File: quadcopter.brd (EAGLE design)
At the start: 196 x 196 mm, 65 parts, among them J1 ISP, U1 ATMEGA128RFA1

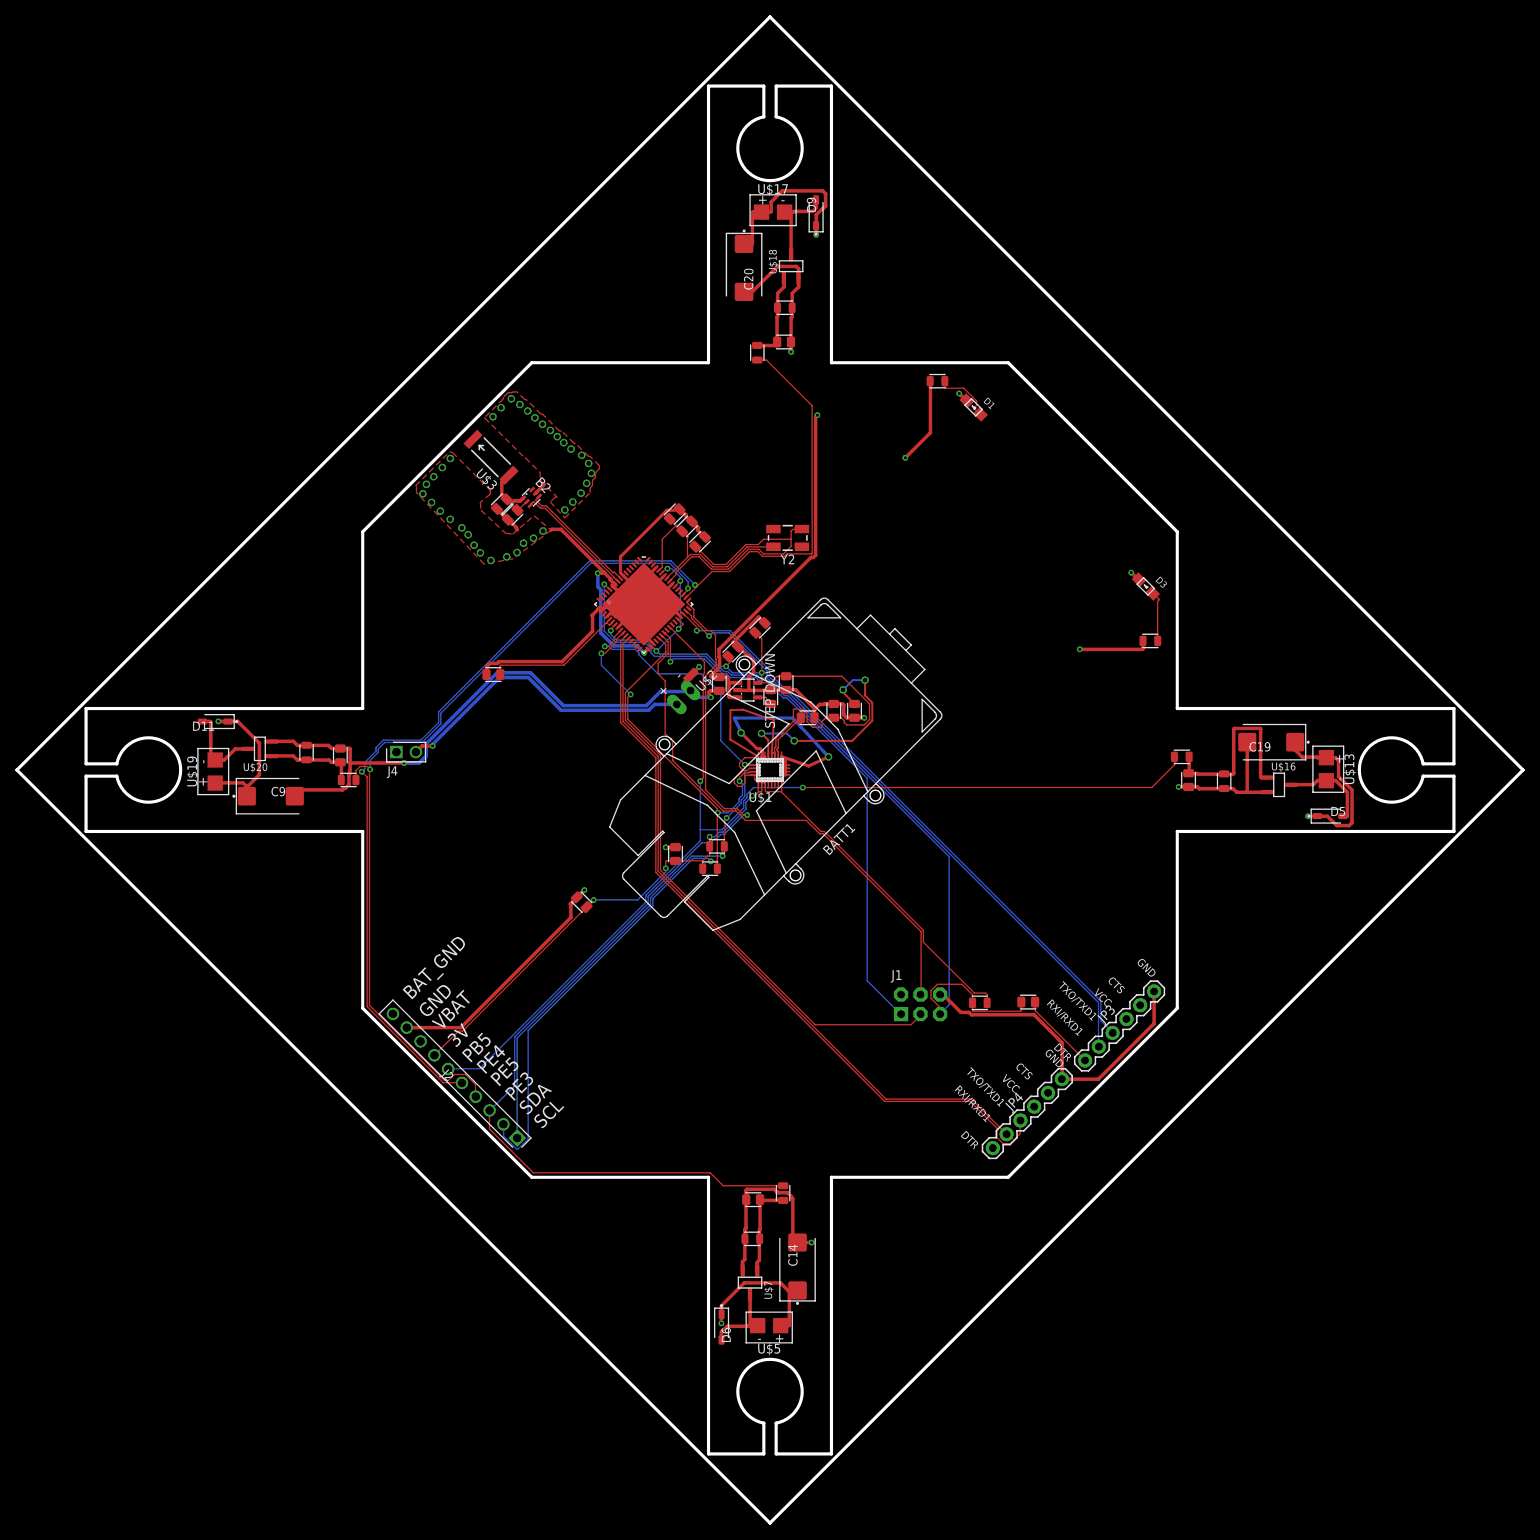
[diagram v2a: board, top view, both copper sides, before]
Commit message: worked on routing more, there are still lots of drc issues though
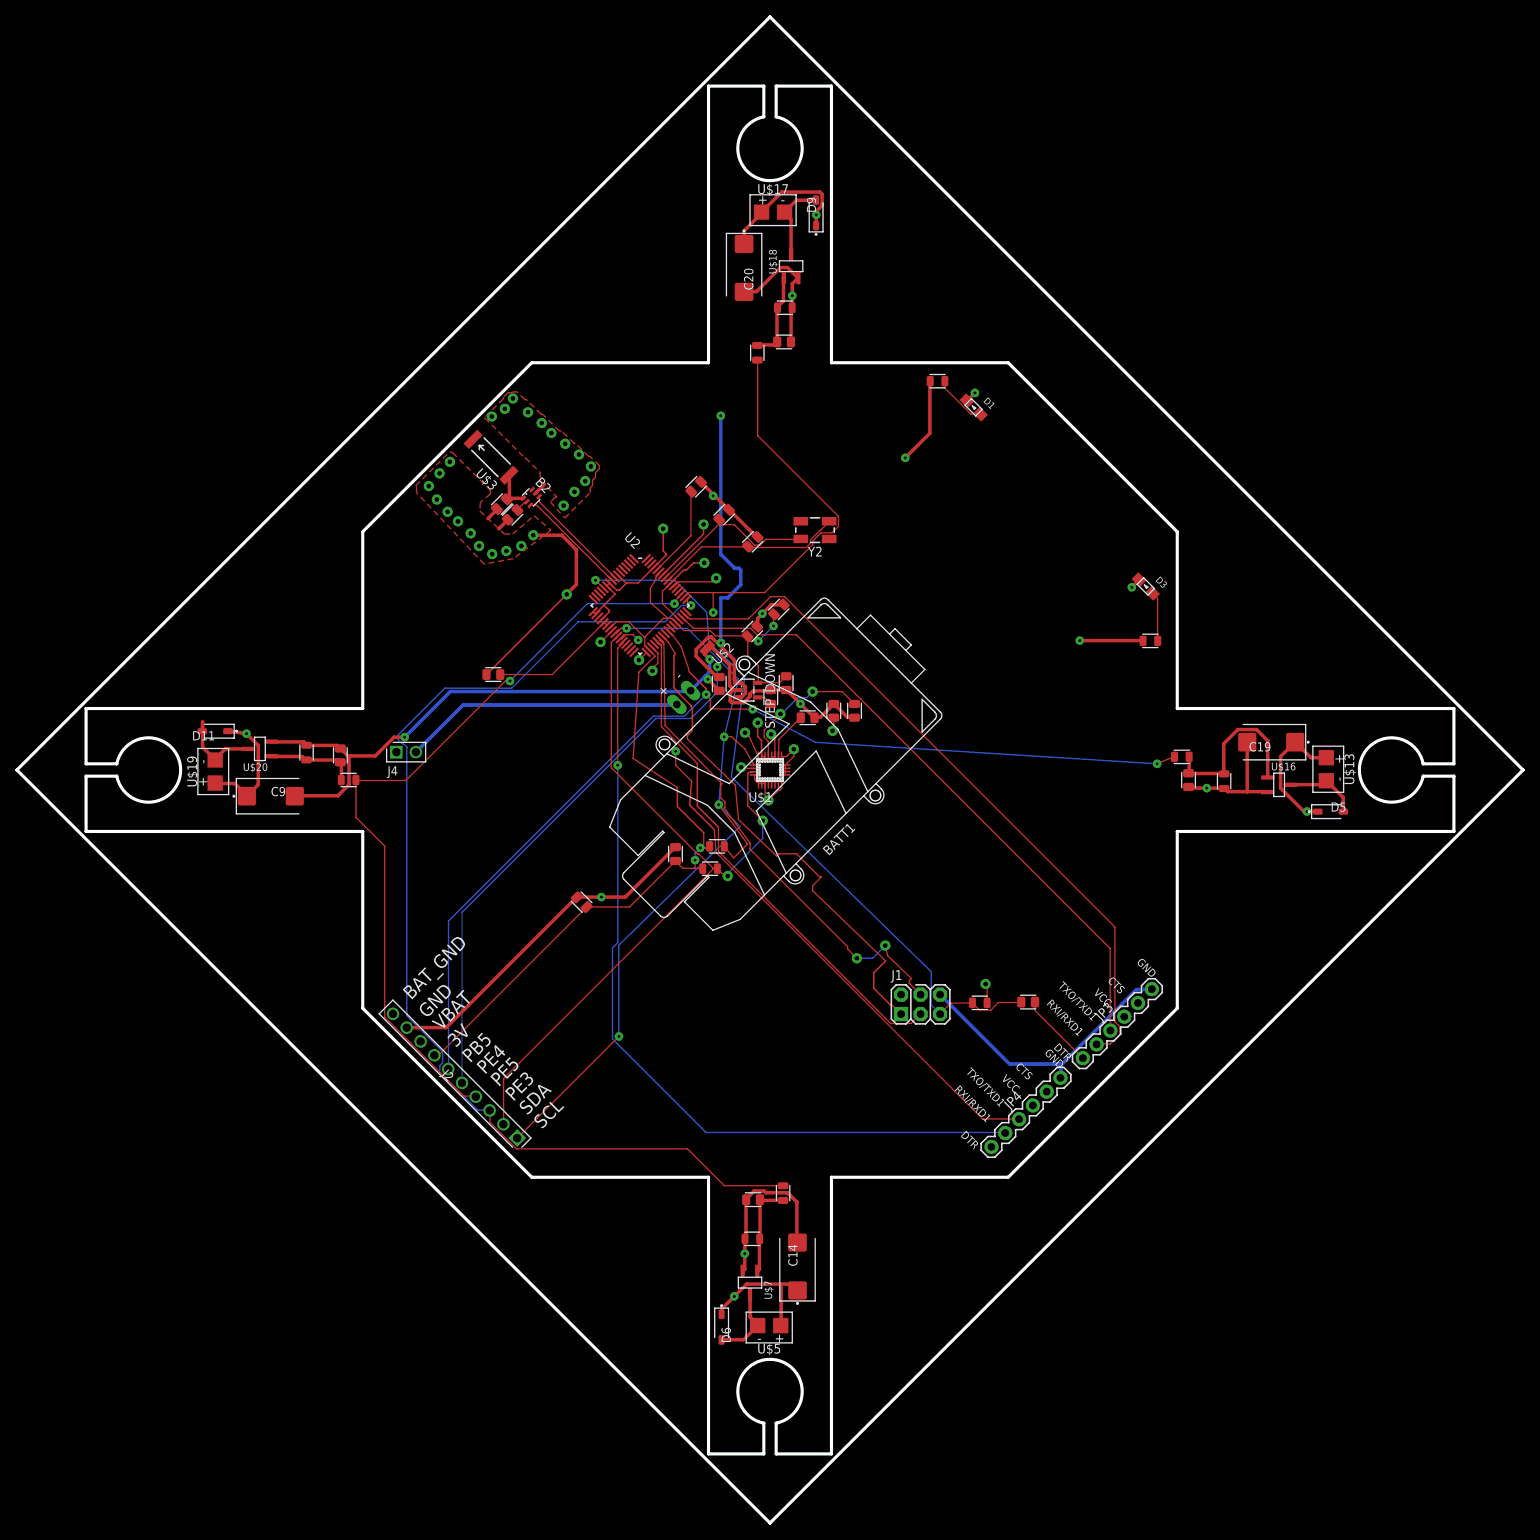
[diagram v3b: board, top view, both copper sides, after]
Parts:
- removed U1: ATMEGA128RFA1, SparkFun-DigitalIC:QFN-64
- added U2: ATMEGA128RFA1, quadparts_prebuilt:QFN-64
- J1: device SparkFun-Connectors:2X3-NS -> quadparts_prebuilt:2X3-NS
- moved C1 6.86 mm to (-2.24, 29.7)
- moved C2 5.06 mm to (-5.97, 33.2)
- moved C6 4.52 mm to (-9.61, 36.9)
- moved U$2 4.15 mm to (-8.15, 15.8)
- moved Y2 3.70 mm to (5.86, 31.2)
- moved C4 3.64 mm to (-2.30, 18.1)
- moved C3 3.43 mm to (1.15, 20.9)
- moved D11 1.25 mm to (-72.2, 5.05)
- moved D5 0.58 mm to (73.0, -5.42)
- moved JP3 0.42 mm to (40.7, -37.5)
- moved JP4 0.24 mm to (28.8, -49.0)
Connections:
- net 3V: now also U2.23, U2.34, U2.44, U2.54, U2.59; no longer U1.23, U1.34, U1.44, U1.54, U1.59
- net A0: now also U2.63; no longer U1.63
- net A1: now also U2.64; no longer U1.64
- net A2: now also U2.1; no longer U1.1
- net A3: now also U2.2; no longer U1.2
- net A4: now also U2.3; no longer U1.3
- net A5: now also U2.4; no longer U1.4
- net A6: now also U2.5; no longer U1.5
- net A7: now also U2.6; no longer U1.6
- net AREF: now also U2.62; no longer U1.62
- net AVDD: now also U2.60; no longer U1.60
- net DVDD: now also U2.21, U2.22; no longer U1.21, U1.22
- net GND: now also U2.10, U2.11, U2.17, U2.18, U2.20, U2.24, U2.33, U2.35, U2.45, U2.55, U2.58, U2.61, U2.7; no longer U1.10, U1.11, U1.17, U1.18, U1.20, U1.24, U1.33, U1.35, U1.45, U1.55, U1.58, U1.61, U1.65, U1.7
- net MISO: now also U2.39; no longer U1.39
- net MOSI: now also U2.38; no longer U1.38
- net N$3: now also U2.57; no longer U1.57
- net N$4: now also U2.56; no longer U1.56
- net PB4: now also U2.40; no longer U1.40
- net PB5: now also U2.41; no longer U1.41
- net PB6: now also U2.42; no longer U1.42
- net PB7: now also U2.43; no longer U1.43
- net PD4: now also U2.29; no longer U1.29
- net PD5: now also U2.30; no longer U1.30
- net PD6: now also U2.31; no longer U1.31
- net PD7: now also U2.32; no longer U1.32
- net PE2: now also U2.48; no longer U1.48
- net PE3: now also U2.49; no longer U1.49
- net PE4: now also U2.50; no longer U1.50
- net PE5: now also U2.51; no longer U1.51
- net PE6: now also U2.52; no longer U1.52
- net PE7: now also U2.53; no longer U1.53
- net PG0: now also U2.14; no longer U1.14
- net PG1: now also U2.15; no longer U1.15
- net PG2: now also U2.16; no longer U1.16
- net PG5: now also U2.19; no longer U1.19
- net RESET: now also U2.12; no longer U1.12
- net RFN: now also U2.9; no longer U1.9
- net RFP: now also U2.8; no longer U1.8
- net RSTON: now also U2.13; no longer U1.13
- net RX1: now also U2.27; no longer U1.27
- net RXD1: now also U2.46; no longer U1.46
- net SCK: now also U2.37; no longer U1.37
- net SCL: now also U2.25; no longer U1.25
- net SDA: now also U2.26; no longer U1.26
- net SSN: now also U2.36; no longer U1.36
- net TX1: now also U2.28; no longer U1.28
- net TXD1: now also U2.47; no longer U1.47
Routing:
- net 3V: track 230.1 -> 157.3 mm
- net GND: track 277.7 -> 241.5 mm, vias 46 -> 39
- net PE4: track 153.3 -> 130.6 mm
- net TX1: track 92.1 -> 108.5 mm, vias 0 -> 1
- net N$4: track 38.0 -> 24.6 mm
- net PE3: track 131.3 -> 144.3 mm
- net SCL: track 96.2 -> 109.0 mm
- net N$5: track 30.8 -> 18.2 mm, vias 4 -> 2
- net TXD1: track 81.3 -> 93.1 mm, vias 1 -> 0
- net SCK: track 77.5 -> 66.8 mm
- net BAT_GND: track 147.5 -> 136.7 mm, vias 5 -> 6
- net PE5: track 111.7 -> 101.2 mm
- net RX1: track 98.0 -> 88.5 mm, vias 0 -> 2
- net RESET: track 104.8 -> 95.7 mm
- net VBAT: track 134.7 -> 125.6 mm, vias 7 -> 8
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
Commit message: autorouting works, things are good
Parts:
- moved C27 26.8 mm to (-32.5, 4.40)
- moved STEP_DOWN 26.4 mm to (-28.4, 3.60)
- moved C13 25.9 mm to (-24.9, 2.60)
- moved J4 22.3 mm to (-26.7, -1.97)
- moved C28 21.6 mm to (-22.8, 4.35), turned to 270 degrees
- moved U$2 20.8 mm to (-27.4, 8.00), turned to 45 degrees
- moved C11 16.0 mm to (-5.35, 3.50), turned to 135 degrees
- moved C18 15.2 mm to (-3.95, 4.90), turned to 315 degrees
- moved Y2 13.3 mm to (-7.09, 28.3), turned to 135 degrees
- moved C16 10.9 mm to (-2.55, 6.30), turned to 135 degrees
- moved C5 9.01 mm to (-28.3, 17.1), turned to 225 degrees
- moved C12 8.21 mm to (26.3, -34.0)
- moved C3 5.92 mm to (-3.95, 23.9), turned to 135 degrees
- moved C6 5.63 mm to (-11.5, 31.6), turned to 135 degrees
- moved R7 5.42 mm to (-6.95, -7.49)
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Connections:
- net BAT_GND: now also C13.2, C28.2, STEP_DOWN.2
- net GND: no longer C13.2, C28.2, STEP_DOWN.2
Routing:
- net 3V: track 157.3 -> 244.3 mm, vias 11 -> 5
- net PE5: track 101.2 -> 154.8 mm, vias 2 -> 0
- net GND: track 241.5 -> 197.2 mm, vias 39 -> 24
- net VBAT: track 125.6 -> 87.4 mm, vias 8 -> 7
- net PE4: track 130.6 -> 156.7 mm
- net JUMPER_INPUT: track 36.5 -> 22.2 mm
- net TXD1: track 93.1 -> 79.1 mm, vias 0 -> 1
- net TX1: track 108.5 -> 97.0 mm, vias 1 -> 0
- net PB5: track 138.9 -> 150.1 mm, vias 3 -> 1
- net FILTERED: track 22.6 -> 12.8 mm
- net RESET: track 95.7 -> 86.1 mm
- net DVDD: track 16.9 -> 7.31 mm
- net N$3: track 23.2 -> 13.7 mm, vias 0 -> 2
- net SCL: track 109.0 -> 99.4 mm, vias 4 -> 2
- net SDA: track 100.1 -> 90.6 mm
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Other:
- board size 196 x 196 mm -> 178 x 178 mm

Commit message: almost forgot newest board and schematic
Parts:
- added SW1: PUSHBUTTON_SMD-VERTICAL-1, quadparts_prebuilt:TE_FSM8JSMA_HS
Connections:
- net GND: now also SW1.1, SW1.2
- net RESET: now also SW1.3, SW1.4
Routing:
- net RESET: track 86.1 -> 108.1 mm
- net GND: track 197.2 -> 216.0 mm
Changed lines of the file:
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@@
 <attribute name="PRICE" value="10.21" x="-16.9" y="21.4" size="1.778" layer="27" rot="R315" display="off"/>
+</element>
+<element name="SW1" library="quadparts_prebuilt" package="TE_FSM8JSMA_HS" value="PUSHBUTTON_SMD-VERTICAL-1" x="12.55" y="-19.95" rot="R225">
+<attribute name="DIST" value="Digikey" x="12.55" y="-19.95" size="1.778" layer="27" rot="R225" display="off"/>
+<attribute name="DISTPN" value="450-1129-ND" x="12.55" y="-19.95" size="1.778" layer="27" rot="R225" display="off"/>
+<attribute name="MFR" value="TE Connectivity Alcoswitch Switches" x="12.55" y="-19.95" size="1.778" layer="27" rot="R225" display="off"/>
+<attribute name="MPN" value="FSM4JSMA" x="12.55" y="-19.95" size="1.778" layer="27" rot="R225" display="off"/>
 </element>
 </elements>
@@
 <wire x1="-28" y1="7.75" x2="-27.803553125" y2="7.64644375" width="0.1524" layer="1"/>
 <wire x1="-28.75" y1="16.25" x2="-28.932859375" y2="16.4671375" width="0.1524" layer="1"/>
+<contactref element="SW1" pad="2"/>
+<contactref element="SW1" pad="1"/>
+<wire x1="11" y1="-15.25" x2="17.25" y2="-21.5" width="0.1524" layer="1"/>
+<wire x1="17.25" y1="-21.5" x2="17.358325" y2="-21.57634375" width="0.1524" layer="1"/>
+<wire x1="11" y1="-15.25" x2="10.923653125" y2="-15.141671875" width="0.1524" layer="1"/>
+<wire x1="17.5" y1="-24.5" x2="17.5" y2="-21.75" width="0.1524" layer="1"/>
+<wire x1="22" y1="-29" x2="17.5" y2="-24.5" width="0.1524" layer="1"/>
+<wire x1="17.5" y1="-21.75" x2="17.358325" y2="-21.57634375" width="0.1524" layer="1"/>
+<wire x1="22" y1="-29" x2="22.14" y2="-29.23" width="0.1524" layer="1"/>
 </signal>
 <signal name="N$3">
@@
 <wire x1="22.25" y1="-32" x2="22.14" y2="-31.77" width="0.1524" layer="1"/>
 <via x="-14.75" y="19.75" extent="1-16" drill="0.381"/>
+<contactref element="SW1" pad="4"/>
+<contactref element="SW1" pad="3"/>
+<wire x1="14" y1="-24.75" x2="7.75" y2="-18.5" width="0.1524" layer="1"/>
+<wire x1="7.75" y1="-18.5" x2="7.741671875" y2="-18.323653125" width="0.1524" layer="1"/>
+<wire x1="14" y1="-24.75" x2="14.17634375" y2="-24.758325" width="0.1524" layer="1"/>
+<wire x1="14.25" y1="-28.25" x2="14.25" y2="-25" width="0.1524" layer="1"/>
+<wire x1="16.5" y1="-30.5" x2="14.25" y2="-28.25" width="0.1524" layer="1"/>
+<wire x1="20.75" y1="-30.5" x2="16.5" y2="-30.5" width="0.1524" layer="1"/>
+<wire x1="22" y1="-31.75" x2="20.75" y2="-30.5" width="0.1524" layer="1"/>
+<wire x1="14.25" y1="-25" x2="14.17634375" y2="-24.758325" width="0.1524" layer="1"/>
+<wire x1="22" y1="-31.75" x2="22.14" y2="-31.77" width="0.1524" layer="1"/>
 </signal>
 <signal name="PE5">
